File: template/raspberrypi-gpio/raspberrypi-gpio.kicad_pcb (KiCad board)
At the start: 2 copper layers, 85 x 56 mm, 1 part, among them P1 CONN_13X2

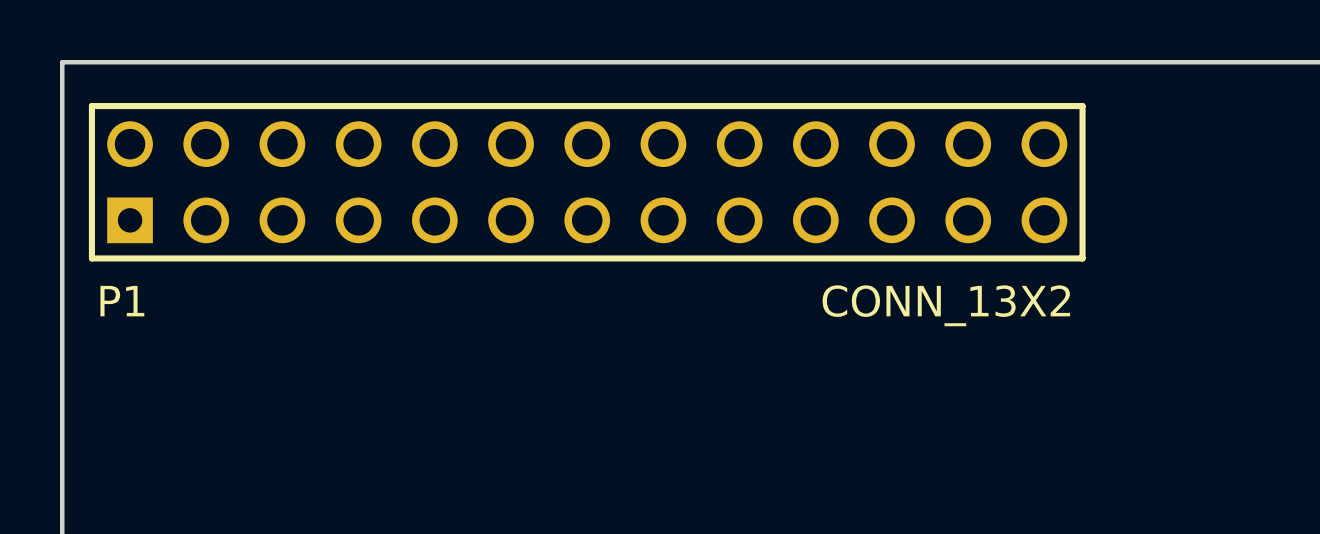
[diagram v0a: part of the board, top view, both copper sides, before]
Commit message: fix template
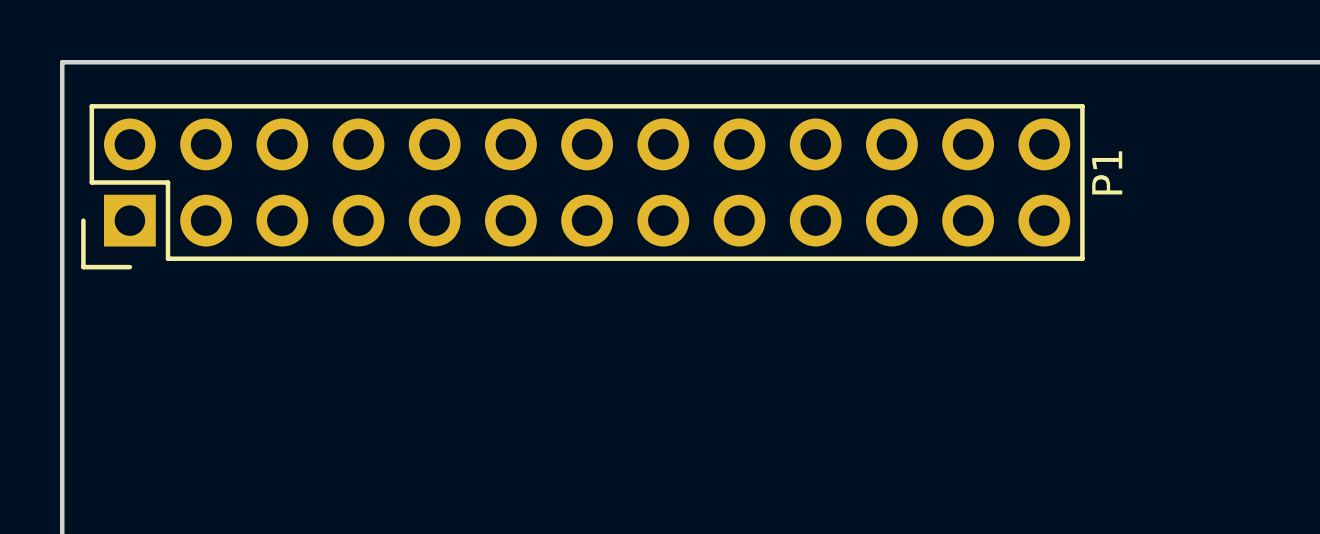
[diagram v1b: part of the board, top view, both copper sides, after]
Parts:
- P1: footprint pin_array_13x2 -> Pin_Headers:Pin_Header_Straight_2x13
- moved P1 15.3 mm to (145.8, 130.3), turned to 90 degrees
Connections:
- net +3.3V renamed +3V3
- P1 pad 10: (no net) -> /RXD
- P1 pad 11: (no net) -> /GPIO17
- P1 pad 12: (no net) -> /GPIO18
- P1 pad 13: (no net) -> /GPIO21
- P1 pad 14: (no net) -> Net-(P1-Pad14)
- P1 pad 15: (no net) -> /GPIO22
- P1 pad 16: (no net) -> /GPIO23
- P1 pad 17: (no net) -> Net-(P1-Pad17)
- P1 pad 18: (no net) -> /GPIO24
- P1 pad 19: (no net) -> /GPIO10(MOSI)
- P1 pad 20: (no net) -> Net-(P1-Pad20)
- P1 pad 21: (no net) -> /GPIO9(MISO)
- P1 pad 22: (no net) -> /GPIO25
- P1 pad 23: (no net) -> /GPIO11(SCLK)
- P1 pad 24: (no net) -> /GPIO8(CE0)
- P1 pad 25: (no net) -> Net-(P1-Pad25)
- P1 pad 26: (no net) -> /GPIO7(CE1)
- P1 pad 3: (no net) -> /GPIO0(SDA)
- P1 pad 4: (no net) -> Net-(P1-Pad4)
- P1 pad 5: (no net) -> /GPIO1(SCL)
- P1 pad 7: (no net) -> /GPIO4
- P1 pad 8: (no net) -> /TXD
- P1 pad 9: (no net) -> Net-(P1-Pad9)
